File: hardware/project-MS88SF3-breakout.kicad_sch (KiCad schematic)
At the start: 27 parts, among them J1 Conn_02x05_Odd_Even, J2 S2B-PH-SM4-TB(LF)(SN), J3 USB4105-GF-A, J4 Conn_01x12_Pin, J5 Conn_01x16_Pin, SW1 PTS810_SJM_250_SMTR_LFS, U1 MS88SF3_NRF52840

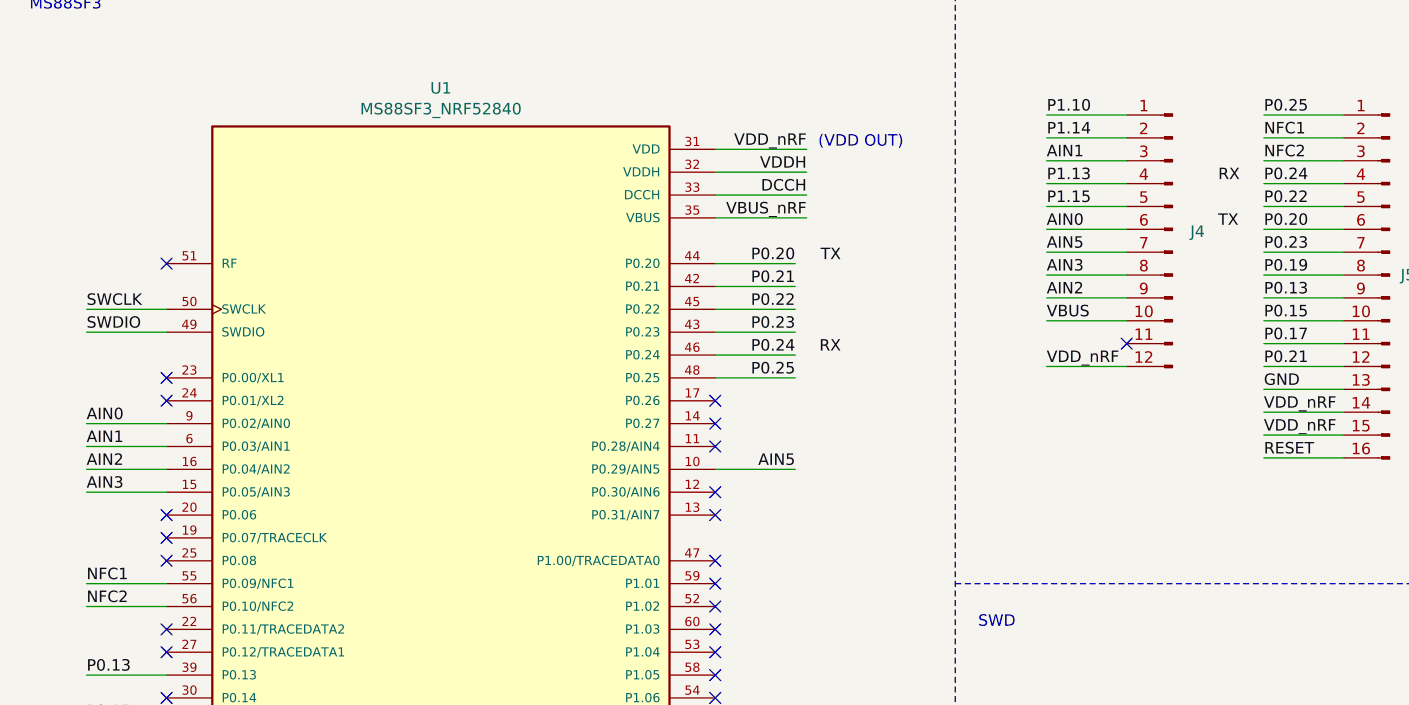
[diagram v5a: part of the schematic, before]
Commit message: Change swd RX/TX to easier pins to route
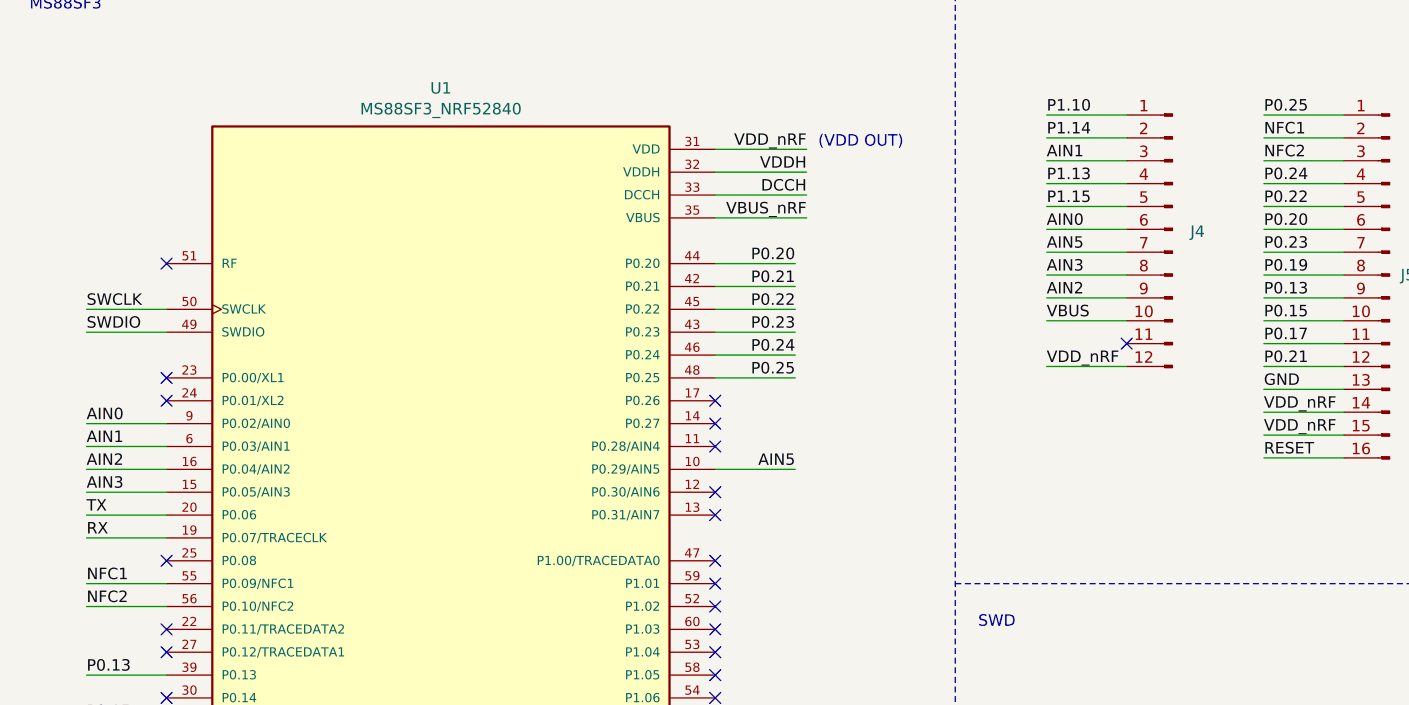
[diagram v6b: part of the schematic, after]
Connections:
- net RX: now also U1.19 (P0.07/TRACECLK)
- net TX: now also U1.20 (P0.06)
- no-connect marks 31 -> 29
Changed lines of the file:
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@@
-	)
-	(no_connect
-		(at 30.48 76.2)
 	)
 	(no_connect
@@
 	)
 	(no_connect
-		(at 30.48 73.66)
-	)
-	(no_connect
 		(at 91.44 99.06)
 	)
@@
 	(wire
 		(pts
+			(xy 21.59 76.2) (xy 30.48 76.2)
+		)
+		(stroke
+			(width 0)
+			(type default)
+		)
+	)
+	(wire
+		(pts
 			(xy 21.59 68.58) (xy 30.48 68.58)
 		)
@@
 		(pts
 			(xy 92.71 123.19) (xy 92.71 121.92)
+		)
+		(stroke
+			(width 0)
+			(type default)
+		)
+	)
+	(wire
+		(pts
+			(xy 21.59 73.66) (xy 30.48 73.66)
 		)
 		(stroke
@@
 		)
 	)
-	(label "TX"
-		(at 147.32 41.91 0)
-		(fields_autoplaced yes)
-		(effects
-			(font
-				(size 1.27 1.27)
-			)
-			(justify left bottom)
-		)
-	)
 	(label "GND"
 		(at 133.35 115.57 0)
@@
 	)
 	(label "TX"
-		(at 105.41 45.72 180)
-		(fields_autoplaced yes)
-		(effects
-			(font
-				(size 1.27 1.27)
-			)
-			(justify right bottom)
+		(at 21.59 73.66 0)
+		(fields_autoplaced yes)
+		(effects
+			(font
+				(size 1.27 1.27)
+			)
+			(justify left bottom)
 		)
 	)
@@
 	)
 	(label "RX"
-		(at 105.41 55.88 180)
-		(fields_autoplaced yes)
-		(effects
-			(font
-				(size 1.27 1.27)
-			)
-			(justify right bottom)
+		(at 21.59 76.2 0)
+		(fields_autoplaced yes)
+		(effects
+			(font
+				(size 1.27 1.27)
+			)
+			(justify left bottom)
 		)
 	)
@@
 		(fields_autoplaced yes)
 		(effects
-			(font
-				(size 1.27 1.27)
-			)
-			(justify left bottom)
-		)
-	)
-	(label "RX"
-		(at 147.32 36.83 0)
-		(fields_autoplaced yes)
-		(effects

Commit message: Change 12/16 pin header footprint
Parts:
- J4: footprint Connector_PinHeader_2.54mm:PinHeader_1x12_P2.54mm_Vertical -> mine:PinHeader_1x12_P2.54mm_Vertical
- J5: footprint Connector_PinHeader_2.54mm:PinHeader_1x16_P2.54mm_Vertical -> mine:PinHeader_1x16_P2.54mm_Vertical
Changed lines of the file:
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@@
 			)
 		)
-		(property "Footprint" "Connector_PinHeader_2.54mm:PinHeader_1x16_P2.54mm_Vertical"
+		(property "Footprint" "mine:PinHeader_1x16_P2.54mm_Vertical"
 			(at 166.37 46.99 0)
 			(effects
@@
 			)
 		)
-		(property "Footprint" "Connector_PinHeader_2.54mm:PinHeader_1x12_P2.54mm_Vertical"
+		(property "Footprint" "mine:PinHeader_1x12_P2.54mm_Vertical"
 			(at 142.24 41.91 0)
 			(effects

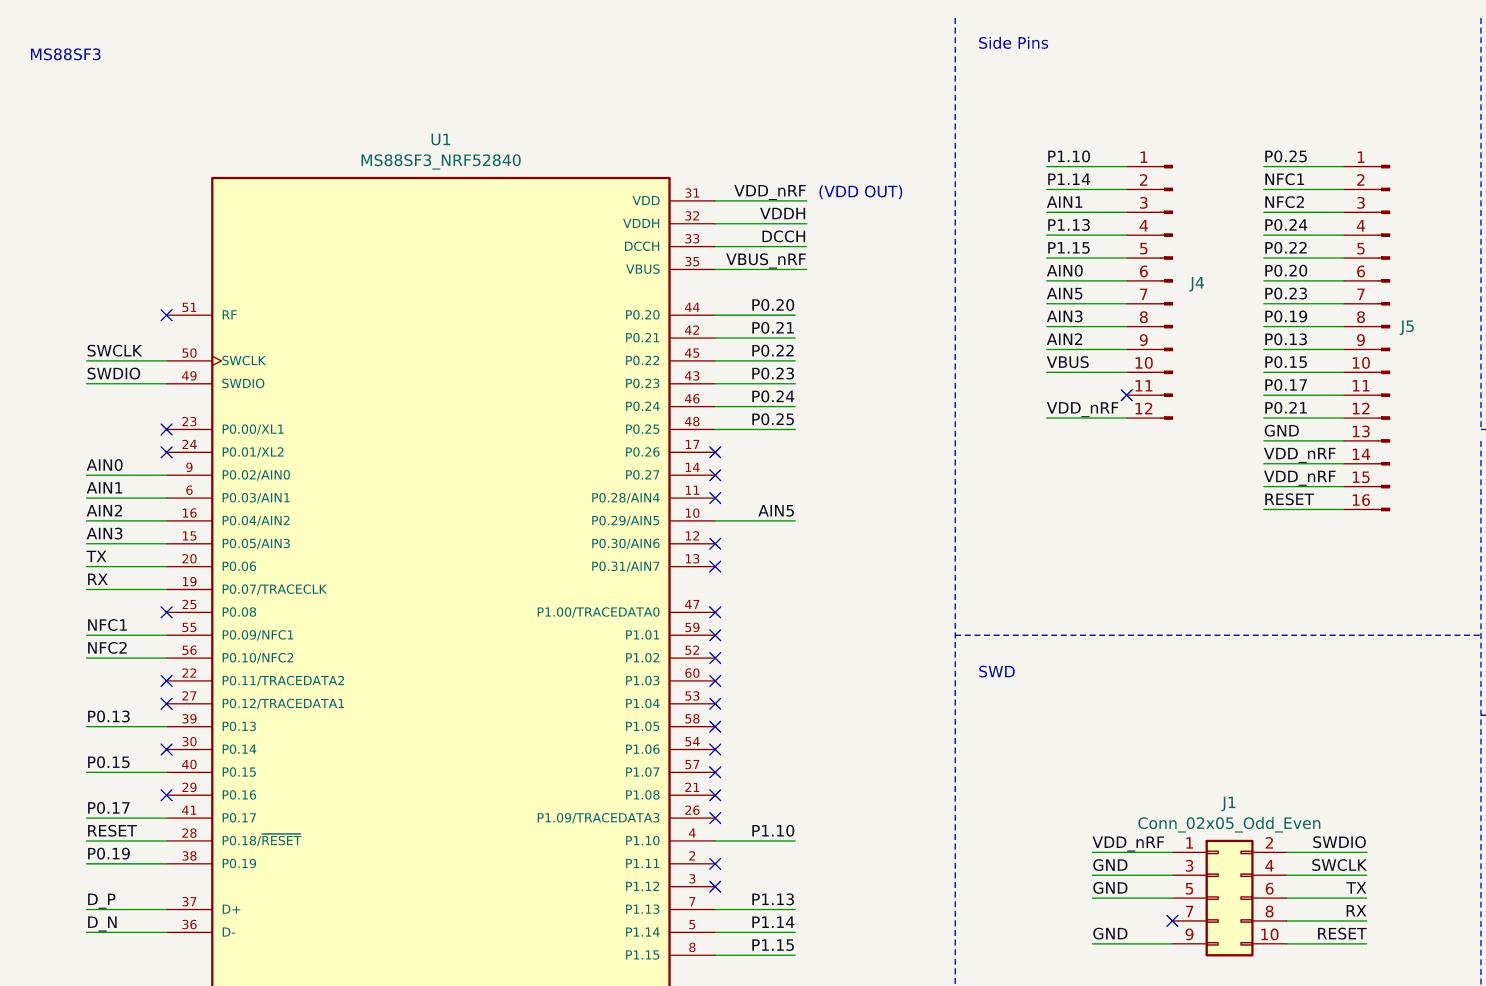
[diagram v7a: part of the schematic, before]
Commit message: Update half the pins in the schematic
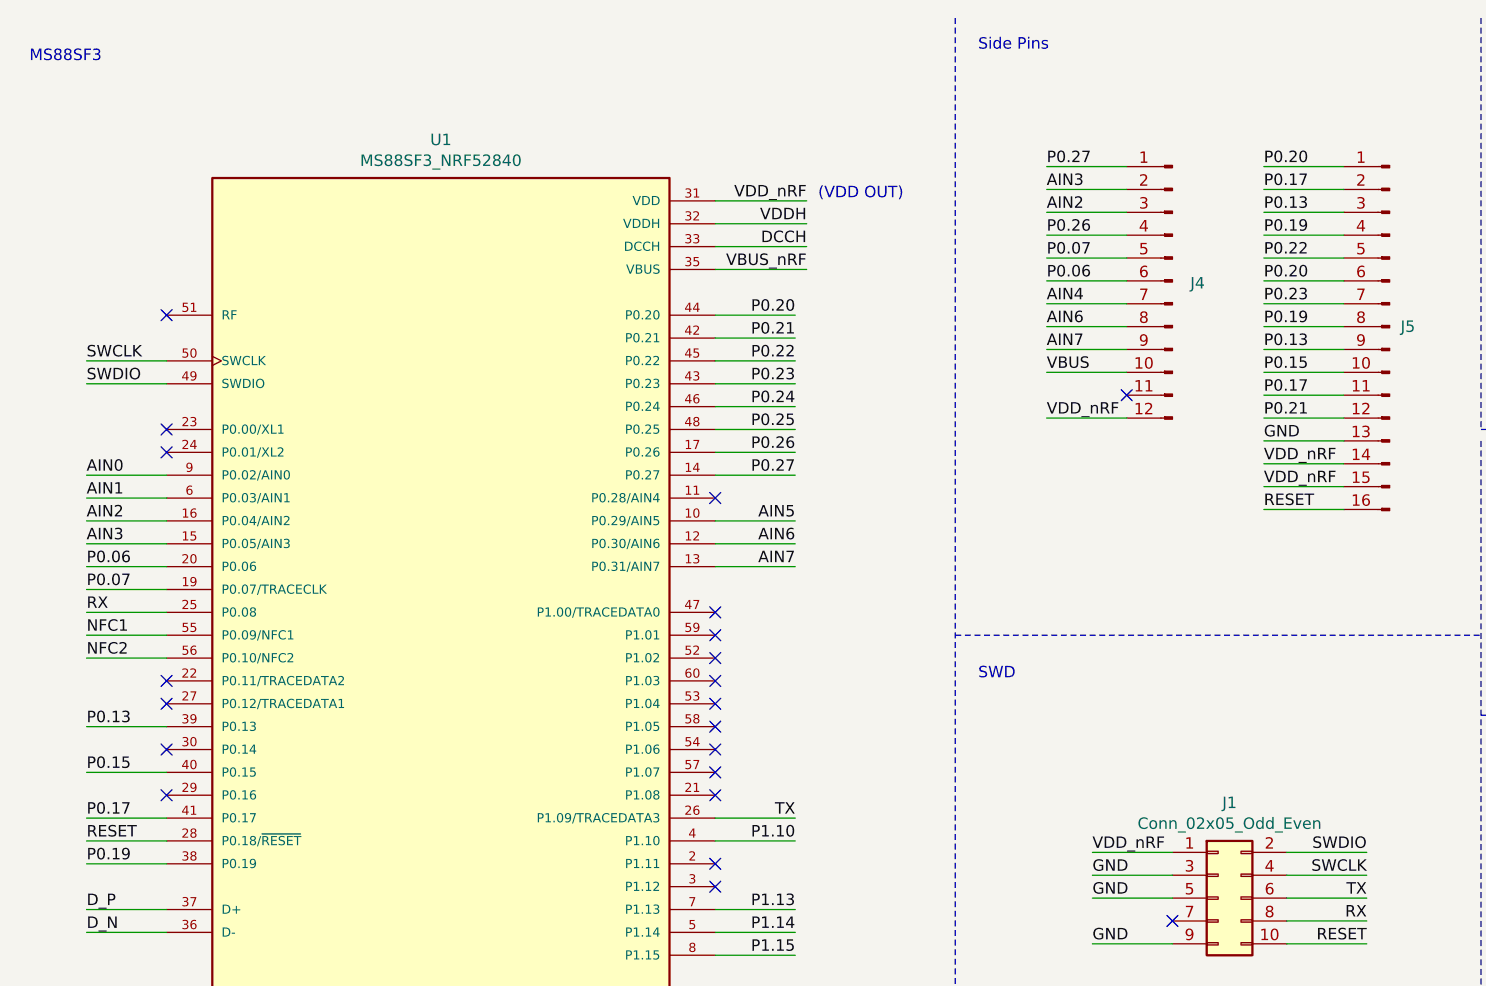
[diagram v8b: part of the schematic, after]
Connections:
- net AIN0: no longer J4.6 (Pin_6)
- net AIN1: no longer J4.3 (Pin_3)
- net AIN2: now also J4.3 (Pin_3); no longer J4.9 (Pin_9)
- net AIN3: now also J4.2 (Pin_2); no longer J4.8 (Pin_8)
- net AIN5: no longer J4.7 (Pin_7)
- net NFC1: no longer J5.2 (Pin_2)
- net NFC2: no longer J5.3 (Pin_3)
- net P0.13: now also J5.3 (Pin_3)
- net P0.17: now also J5.2 (Pin_2)
- net P0.19: now also J5.4 (Pin_4)
- net P0.20: now also J5.1 (Pin_1)
- net P0.24: no longer J5.4 (Pin_4)
- net P0.25: no longer J5.1 (Pin_1)
- net P1.10: no longer J4.1 (Pin_1)
- net P1.13: no longer J4.4 (Pin_4)
- net P1.14: no longer J4.2 (Pin_2)
- net P1.15: no longer J4.5 (Pin_5)
- net RX: now also U1.25 (P0.08); no longer U1.19 (P0.07/TRACECLK)
- net TX: now also U1.26 (P1.09/TRACEDATA3); no longer U1.20 (P0.06)
- net AIN6: now reaches U1.12 (P0.30/AIN6)
- net AIN6: now also J4.8 (Pin_8)
- net AIN7: now reaches U1.13 (P0.31/AIN7)
- net AIN7: now also J4.9 (Pin_9)
- net P0.27: now reaches U1.14 (P0.27)
- net P0.27: now also J4.1 (Pin_1)
- net P0.26: now reaches U1.17 (P0.26)
- net P0.26: now also J4.4 (Pin_4)
- new net AIN4: J4.7 (Pin_7)
- new net P0.06: J4.6 (Pin_6), U1.20 (P0.06)
- new net P0.07: J4.5 (Pin_5), U1.19 (P0.07/TRACECLK)
- no-connect marks 29 -> 23
